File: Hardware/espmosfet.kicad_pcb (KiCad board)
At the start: 2 copper layers, 32 x 42 mm, 58 parts, among them J1 USB_B_Micro, J2 Conn_01x04_Male, J3 USB_A, J4 Conn_01x04_Male, J5 Conn_01x02_Male, J6 Conn_01x02_Male, J7 Conn_01x03_Male, P1 USB_C_Receptacle_USB2.0, P2 USB_C_Receptacle_USB2.0, Q1 AO3400A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

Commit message: adjust Readme
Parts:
- added JP1: Jumper_2_Open, Jumper:SolderJumper-2_P1.3mm_Open_Pad1.0x1.5mm, F.Cu at (98.5, 116.9)
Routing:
- net Net-(D5-Pad2): track 11.9 -> 17.0 mm
- net Net-(D5-Pad4): track 5.68 -> 7.59 mm
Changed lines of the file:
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@@
   (net 41 "+12V")
   (net 42 "Net-(D5-Pad4)")
-  (net 43 "Net-(R17-Pad2)")
+  (net 43 "Net-(U5-Pad3)")
   (net 44 "/GPIO2")
   (net 45 "/Shield")
@@
     )
   )
+  (footprint "Jumper:SolderJumper-2_P1.3mm_Open_Pad1.0x1.5mm" (layer "F.Cu")
+    (at 98.45 116.9 -90)
+    (descr "SMD Solder Jumper, 1x1.5mm Pads, 0.3mm gap, open")
+    (tags "solder jumper open")
+    (property "Sheetfile" "espmosfet.kicad_sch")
+    (property "Sheetname" "")
+    (attr exclude_from_pos_files)
+    (fp_text reference "JP1" (at 0.7 -1.6 90) (layer "F.SilkS")
+      (effects (font (size 0.7 0.7) (thickness 0.1)))
+    )
+    (fp_text value "Jumper_2_Open" (at 0 1.9 90) (layer "F.Fab")
+      (effects (font (size 1 1) (thickness 0.15)))
+    )
+    (fp_line (start 1.4 -1) (end 1.4 1) (layer "F.SilkS") (width 0.12))
+    (fp_line (start -1.4 -1) (end 1.4 -1) (layer "F.SilkS") (width 0.12))
+    (fp_line (start -1.4 1) (end -1.4 -1) (layer "F.SilkS") (width 0.12))
+    (fp_line (start 1.4 1) (end -1.4 1) (layer "F.SilkS") (width 0.12))
+    (fp_line (start -1.65 -1.25) (end 1.65 -1.25) (layer "F.CrtYd") (width 0.05))
+    (fp_line (start 1.65 1.25) (end -1.65 1.25) (layer "F.CrtYd") (width 0.05))
+    (fp_line (start 1.65 1.25) (end 1.65 -1.25) (layer "F.CrtYd") (width 0.05))
+    (fp_line (start -1.65 -1.25) (end -1.65 1.25) (layer "F.CrtYd") (width 0.05))
+    (pad "1" smd rect locked (at -0.65 0 270) (size 1 1.5) (layers "F.Cu" "F.Mask")
+      (net 53 "Net-(D5-Pad2)") (pinfunction "A") (pintype "passive"))
+    (pad "2" smd rect locked (at 0.65 0 270) (size 1 1.5) (layers "F.Cu" "F.Mask")
+      (net 42 "Net-(D5-Pad4)") (pinfunction "B") (pintype "passive"))
+  )
   (footprint "Button_Switch_SMD:SW_Push_SPST_NO_Alps_SKRK" (layer "F.Cu")
     (at 107 120.6)
@@
       (net 42 "Net-(D5-Pad4)") (pintype "passive"))
     (pad "2" smd roundrect locked (at 0.9125 0 270) (size 1.025 1.4) (layers "F.Cu" "F.Paste" "F.Mask") (roundrect_rratio 0.243902)
-      (net 43 "Net-(R17-Pad2)") (pintype "passive"))
+      (net 43 "Net-(U5-Pad3)") (pintype "passive"))
     (model "${KICAD6_3DMODEL_DIR}/Resistor_SMD.3dshapes/R_0805_2012Metric.wrl"
       (offset (xyz 0 0 0))
@@
     (property "Sheetname" "")
     (attr smd)
-    (fp_text reference "D5" (at 4.3 -2.65 90) (layer "F.SilkS")
+    (fp_text reference "D5" (at 4.3 2.95 90) (layer "F.SilkS")
       (effects (font (size 0.7 0.7) (thickness 0.1)))
     )
@@
       (net 9 "GND") (pinfunction "GND") (pintype "power_in"))
     (pad "3" smd roundrect locked (at -1.1375 0.95 270) (size 1.325 0.6) (layers "F.Cu" "F.Paste" "F.Mask") (roundrect_rratio 0.25)
-      (net 43 "Net-(R17-Pad2)") (pinfunction "A") (pintype "bidirectional"))
+      (net 43 "Net-(U5-Pad3)") (pinfunction "A") (pintype "bidirectional"))
     (pad "4" smd roundrect locked (at 1.1375 0.95 270) (size 1.325 0.6) (layers "F.Cu" "F.Paste" "F.Mask") (roundrect_rratio 0.25)
       (net 44 "/GPIO2") (pinfunction "B") (pintype "bidirectional"))
@@
     (property "Sheetname" "")
     (attr through_hole)
-    (fp_text reference "J7" (at 2.4 0.2) (layer "F.SilkS")
+    (fp_text reference "J7" (at -1.65 7.45) (layer "F.SilkS")
       (effects (font (size 0.7 0.7) (thickness 0.1)))
     )
@@
   (segment (start 120.27548 141.32452) (end 118.19952 141.32452) (width 0.5) (layer "B.Cu") (net 41))
   (segment (start 115.6 141.55) (end 117.575 141.55) (width 0.35) (layer "B.Cu") (net 41))
-  (segment (start 98.1 113.85) (end 98.1 119.3875) (width 0.5) (layer "F.Cu") (net 42))
+  (segment (start 98.1 114.1) (end 98.1 113.85) (width 0.5) (layer "F.Cu") (net 42))
+  (segment (start 99.7 116.95) (end 99.7 115.7) (width 0.5) (layer "F.Cu") (net 42))
+  (segment (start 98.2 117.55) (end 99.1 117.55) (width 0.5) (layer "F.Cu") (net 42))
+  (segment (start 99.1 117.55) (end 99.7 116.95) (width 0.5) (layer "F.Cu") (net 42))
   (segment (start 98.1 119.3875) (end 98.2 119.4875) (width 0.5) (layer "F.Cu") (net 42))
+  (segment (start 99.7 115.7) (end 98.1 114.1) (width 0.5) (layer "F.Cu") (net 42))
+  (segment (start 98.2 119.4875) (end 98.2 117.55) (width 0.5) (layer "F.Cu") (net 42))
   (segment (start 99.45 120.4625) (end 100.05 120.4625) (width 0.4) (layer "F.Cu") (net 43))
   (segment (start 99.45 120.4625) (end 98.6 121.3125) (width 0.4) (layer "F.Cu") (net 43))
@@
   (segment (start 114.602445 136.8495) (end 114.602445 136.677445) (width 0.25) (layer "B.Cu") (net 50))
   (segment (start 114.577465 136.82452) (end 114.602445 136.8495) (width 0.25) (layer "B.Cu") (net 50))
+  (segment (start 98.2 116.25) (end 97.1 116.25) (width 0.5) (layer "F.Cu") (net 53))
   (segment (start 93.7 117.84) (end 95.4 119.54) (width 0.4) (layer "F.Cu") (net 53))
+  (segment (start 96.85 116.5) (end 96.85 118.09) (width 0.5) (layer "F.Cu") (net 53))
   (segment (start 93.7 110.15) (end 93.7 117.84) (width 0.4) (layer "F.Cu") (net 53))
+  (segment (start 97.1 116.25) (end 96.85 116.5) (width 0.5) (layer "F.Cu") (net 53))
   (segment (start 95.8525 119.4875) (end 95.8 119.54) (width 0.4) (layer "F.Cu") (net 53))
   (segment (start 94.9 108.95) (end 93.7 110.15) (width 0.4) (layer "F.Cu") (net 53))
+  (segment (start 96.85 118.09) (end 95.4 119.54) (width 0.5) (layer "F.Cu") (net 53))
   (segment (start 123.4 139.6) (end 124.249022 139.6) (width 0.5) (layer "F.Cu") (net 54))
   (segment (start 124.599511 139.249511) (end 124.599511 137.599511) (width 0.5) (layer "F.Cu") (net 54))

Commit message: Update espmosfet.kicad_pcb
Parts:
- added G***: LOGO, LOGO, B.Cu at (119.8, 105.2)
- moved R2 0.66 mm to (114.0, 106.3)
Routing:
- net +3V3: track 106.7 -> 106.0 mm

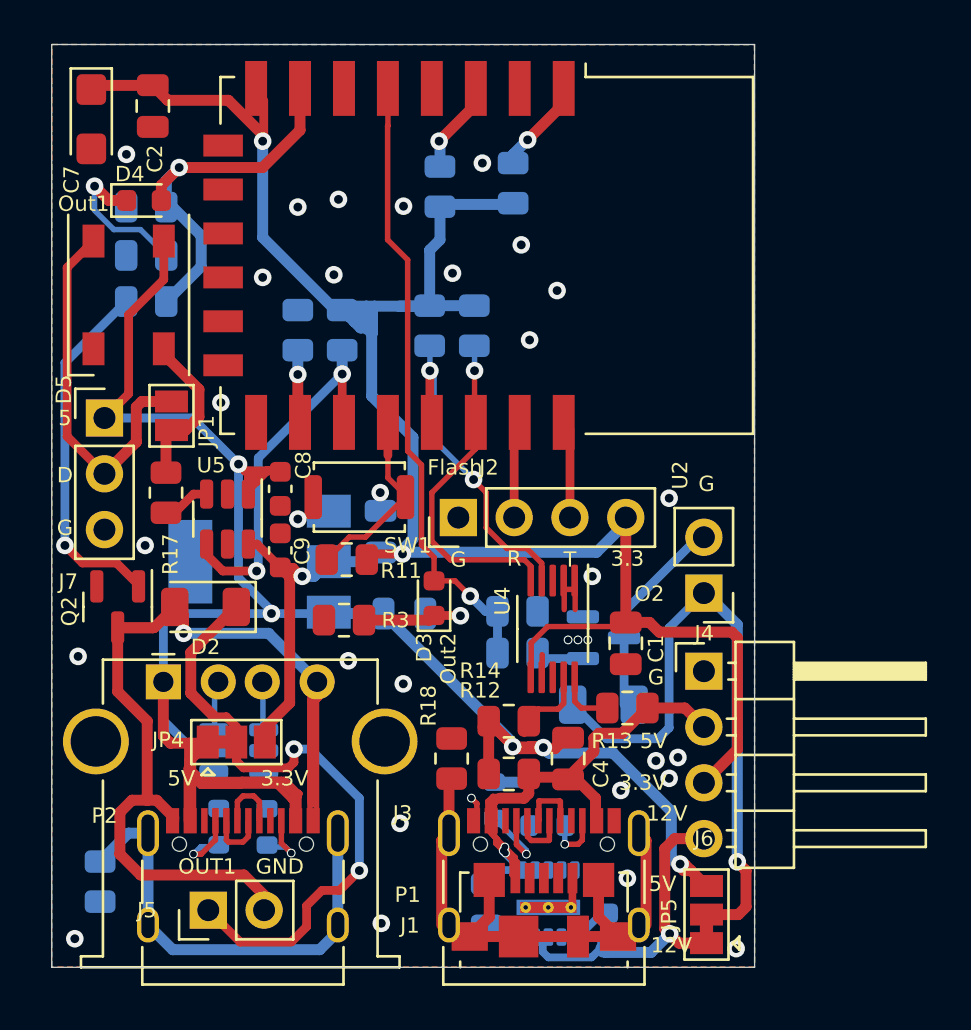
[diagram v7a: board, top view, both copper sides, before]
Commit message: fix ws2812b pinout, change to open jumpers
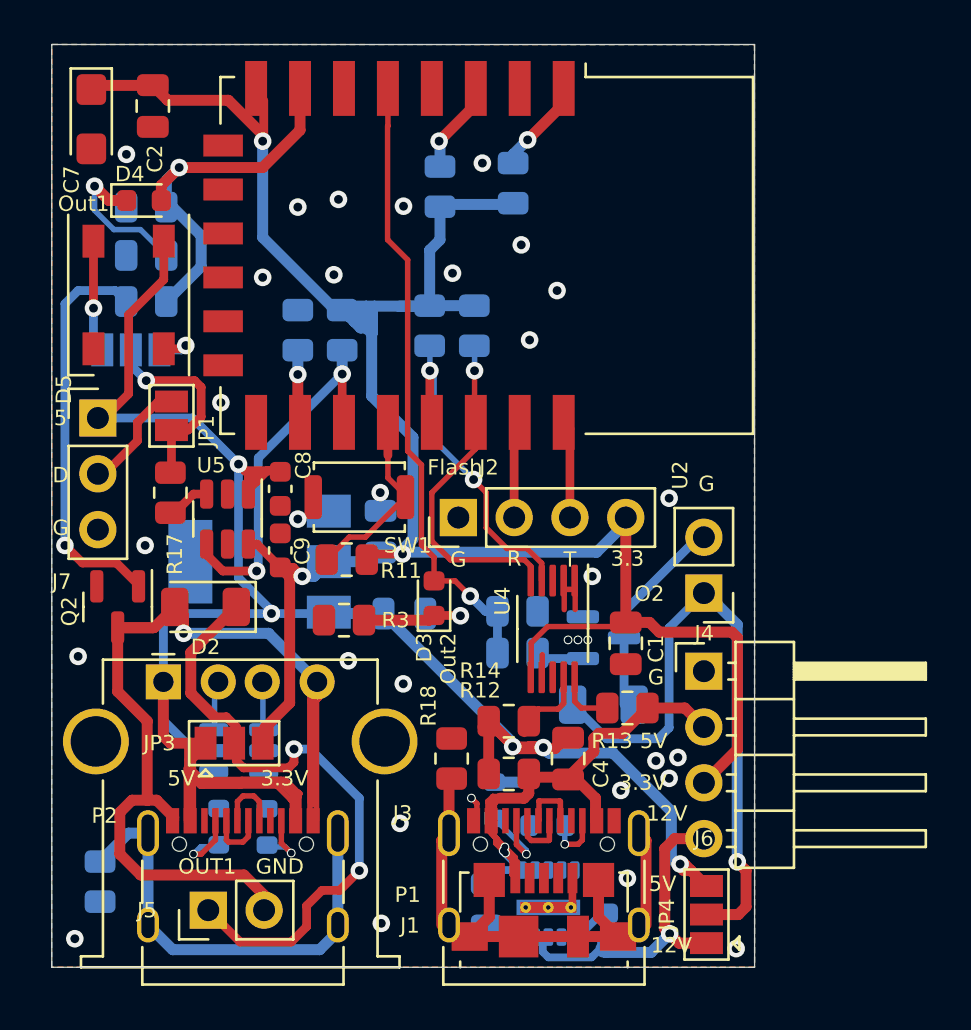
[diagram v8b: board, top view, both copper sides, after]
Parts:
- removed JP5: SolderJumper_3_Bridged12, Jumper:SolderJumper-3_P1.3mm_Bridged12_Pad1.0x1.5mm
- added JP2: Jumper_3_Open, Jumper:SolderJumper-3_P1.3mm_Open_Pad1.0x1.5mm, B.Cu at (96.6, 113.9)
- added JP3: Jumper_3_Open, Jumper:SolderJumper-3_P1.3mm_Open_Pad1.0x1.5mm, F.Cu at (101.3, 131.8)
- JP4: value SolderJumper_3_Bridged12 -> Jumper_3_Open; footprint Jumper:SolderJumper-3_P1.3mm_Bridged12_Pad1.0x1.5mm -> Jumper:SolderJumper-3_P1.3mm_Open_Pad1.0x1.5mm
- moved JP4 22.8 mm to (122.8, 139.6), turned to 90 degrees
- moved J7 0.30 mm to (95.1, 117.0)
- moved R17 0.20 mm to (98.4, 120.4)
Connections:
- D5 pad 2: Net-(D5-Pad2) -> LDOUT
- D5 pad 4: Net-(D5-Pad4) -> LDIN
- J7 pad 2: Net-(D5-Pad2) -> Net-(J7-Pad2)
- JP1 pad 1: Net-(D5-Pad2) -> Net-(J7-Pad2)
- JP1 pad 2: Net-(D5-Pad4) -> DOUT
- JP4 pad 1: +5V -> +12V
- JP4 pad 2: /O1V -> /O2V
- JP4 pad 3: +3V3 -> +5V
- R17 pad 1: Net-(D5-Pad4) -> DOUT
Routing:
- net Net-(D5-Pad2): track 17.0 -> 0.00 mm
- net DOUT: track 0.00 -> 9.44 mm, vias 0 -> 1
- net Net-(D5-Pad4): track 7.59 -> 0.00 mm
- net LDOUT: track 0.00 -> 5.12 mm, vias 0 -> 1
- net Net-(J7-Pad2): track 0.00 -> 4.90 mm
- net LDIN: track 0.00 -> 2.34 mm, vias 0 -> 1
- net Net-(Q2-Pad1): track 16.4 -> 18.3 mm
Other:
- board text added: "ESP-12x USB Mosfet Switch Digital LED control V3"
- board text removed: "ESP-12x USB Mosfet Switch Digital LED control V2"
